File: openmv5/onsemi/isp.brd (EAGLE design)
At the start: 35.6 x 16.5 mm, 61 parts, among them IC1 AP0202AT2L00XPGA0, IC2 MIC5365-2.8YC5-TR, IC3 TLV62568PDDCR, J1 DF12-36-DS, J2 DF12-36-DP, M1 9774030151R, M2 9774030151R, Q1 PMXB120EPEZ

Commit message: Update resistor value
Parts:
- R6: value 1K -> 10K
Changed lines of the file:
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@@
 <attribute name="VALUE" x="12.581" y="8.255" size="0.8128" layer="28" ratio="10" rot="MR270"/>
 </element>
-<element name="R6" library="rcl" library_urn="urn:adsk.eagle:library:334" package="R0402" package3d_urn="urn:adsk.eagle:package:23547/3" value="1K" x="10.287" y="10.795" smashed="yes" rot="MR90">
-<attribute name="MPN" value="CRCW04021K00FKEDC" x="10.287" y="10.795" size="1.778" layer="28" rot="MR90" display="off"/>
+<element name="R6" library="rcl" library_urn="urn:adsk.eagle:library:334" package="R0402" package3d_urn="urn:adsk.eagle:package:23547/3" value="10K" x="10.287" y="10.795" smashed="yes" rot="MR90">
+<attribute name="MPN" value="AC0402FR-1310KL" x="10.287" y="10.795" size="1.778" layer="28" rot="MR90" display="off"/>
 <attribute name="NAME" x="10.922" y="10.16" size="1.27" layer="26" rot="MR90"/>
 <attribute name="POPULARITY" value="34" x="10.287" y="10.795" size="1.778" layer="28" rot="MR90" display="off"/>

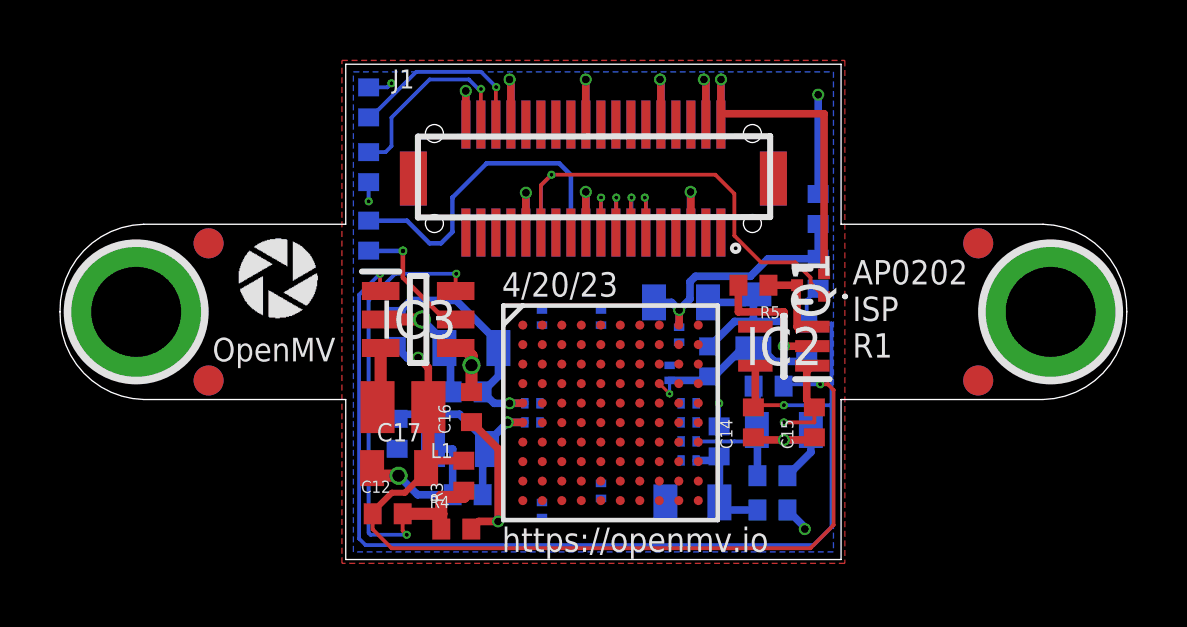
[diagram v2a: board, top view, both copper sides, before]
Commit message: Update camera modules to use different non-flippable pmosfet
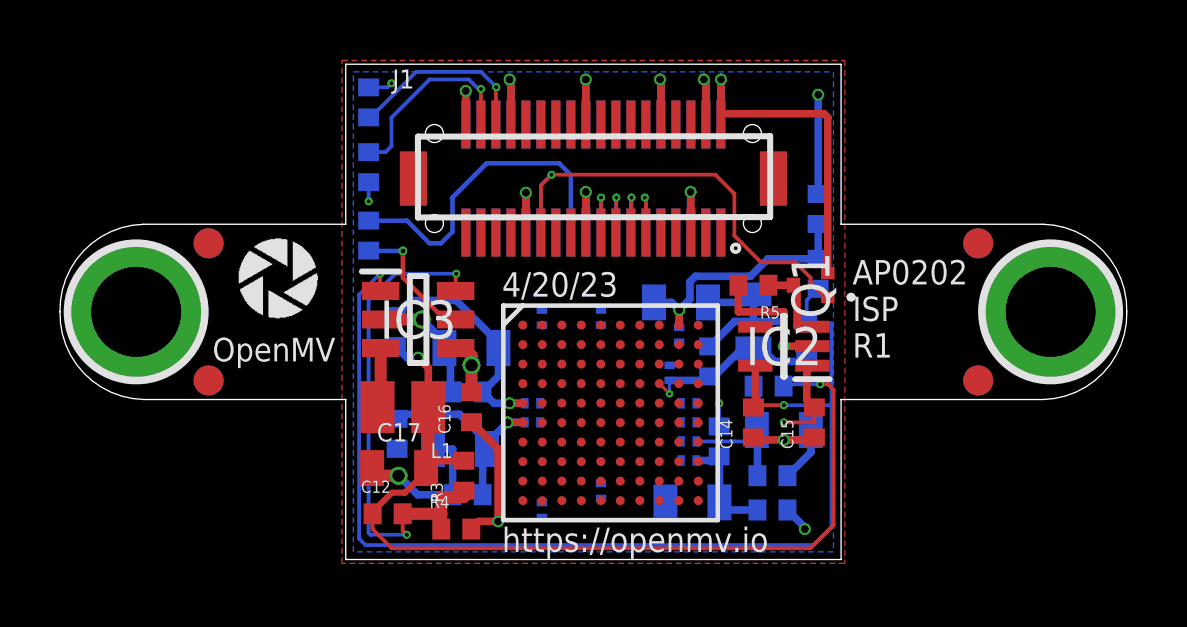
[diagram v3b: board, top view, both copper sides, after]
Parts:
- Q1: value PMXB120EPEZ -> SSM3J15FV,L3F; device PMXB120EPEZ:PMXB120EPEZ -> SSM3J15FV_L3F:SSM3J15FVL3F
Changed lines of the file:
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@@
 <attribute name="VALUE" x="21.082" y="2.794" size="0.6096" layer="28" font="vector" ratio="20" rot="MR180" align="top-center"/>
 </element>
-<element name="Q1" library="PMXB120EPEZ" package="PMXB120EPEZ" value="PMXB120EPEZ" x="25.019" y="9.144" smashed="yes" rot="R90">
-<attribute name="DESCRIPTION" value="MOSFET 30 V, P-channel Trench MOSFET" x="25.019" y="6.096" size="1.778" layer="27" rot="R90" display="off"/>
-<attribute name="HEIGHT" value="0.4mm" x="25.019" y="6.096" size="1.778" layer="27" rot="R90" display="off"/>
-<attribute name="MANUFACTURER_NAME" value="Nexperia" x="25.019" y="6.096" size="1.778" layer="27" rot="R90" display="off"/>
-<attribute name="MANUFACTURER_PART_NUMBER" value="PMXB120EPEZ" x="25.019" y="6.096" size="1.778" layer="27" rot="R90" display="off"/>
-<attribute name="MOUSER_PART_NUMBER" value="771-PMXB120EPEZ" x="25.019" y="6.096" size="1.778" layer="27" rot="R90" display="off"/>
-<attribute name="MOUSER_PRICE-STOCK" value="https://www.mouser.co.uk/ProductDetail/Nexperia/PMXB120EPEZ?qs=gNSudQoqUYCYLaOobF3dPA%3D%3D" x="25.019" y="6.096" size="1.778" layer="27" rot="R90" display="off"/>
-<attribute name="MPN" value="PMXB120EPEZ" x="25.019" y="6.096" size="1.778" layer="27" rot="R90" display="off"/>
+<element name="Q1" library="SSM3J15FV_L3F" package="SSM3J15FVL3F" value="SSM3J15FV,L3F" x="25.019" y="9.144" smashed="yes" rot="R90">
+<attribute name="DESCRIPTION" value="MOSFET Small-signal MOSFET High Speed Switching" x="25.019" y="6.096" size="1.778" layer="27" rot="R90" display="off"/>
+<attribute name="HEIGHT" value="0.55mm" x="25.019" y="6.096" size="1.778" layer="27" rot="R90" display="off"/>
+<attribute name="MANUFACTURER_NAME" value="Toshiba" x="25.019" y="6.096" size="1.778" layer="27" rot="R90" display="off"/>
+<attribute name="MANUFACTURER_PART_NUMBER" value="SSM3J15FV,L3F" x="25.019" y="6.096" size="1.778" layer="27" rot="R90" display="off"/>
+<attribute name="MOUSER_PART_NUMBER" value="757-SSM3J15FVL3F" x="25.019" y="6.096" size="1.778" layer="27" rot="R90" display="off"/>
+<attribute name="MOUSER_PRICE-STOCK" value="https://www.mouser.co.uk/ProductDetail/Toshiba/SSM3J15FVL3F?qs=PDgMCp4xDJb4qTgE7FAUzA%3D%3D" x="25.019" y="6.096" size="1.778" layer="27" rot="R90" display="off"/>
+<attribute name="MPN" value="SSM3J15FV,L3F" x="25.019" y="6.096" size="1.778" layer="27" rot="R90" display="off"/>
 <attribute name="NAME" x="25.019" y="9.144" size="1.27" layer="25" rot="R90" align="center"/>
 <attribute name="VALUE" x="25.019" y="9.144" size="1.27" layer="27" rot="R90" align="center"/>
@@
 </element>
 <element name="J1" library="DF12-36-DS" package="DF12-36-DS" value="DF12-36-DS" x="17.78" y="12.7" smashed="yes">
-<attribute name="MPN" value="DF12NB-36DS-0.5V(51)" x="17.78" y="12.7" size="1.778" layer="27" display="off"/>
+<attribute name="MPN" value="DF12NB(3.0)-36DS-0.5V(51)" x="17.78" y="12.7" size="1.778" layer="27" display="off"/>
 <attribute name="NAME" x="11.08" y="15.7" size="0.635" layer="25"/>
 </element>
@@
 <wire x1="25.146" y1="5.072" x2="24.892" y2="5.326" width="0.254" layer="1"/>
 <wire x1="24.892" y1="6.274" x2="24.892" y2="5.326" width="0.254" layer="1"/>
-<wire x1="25.469" y1="9.519" x2="25.469" y2="14.859" width="0.254" layer="1"/>
 <wire x1="22.03" y1="14.859" x2="22.03" y2="14.5001" width="0.254" layer="1"/>
-<wire x1="25.469" y1="14.859" x2="22.03" y2="14.859" width="0.254" layer="1"/>
+<wire x1="22.03" y1="14.859" x2="25.469" y2="14.859" width="0.254" layer="1"/>
 <wire x1="24.13" y1="4.572" x2="25.146" y2="4.572" width="0.127" layer="1"/>
 <wire x1="25.146" y1="4.572" x2="25.146" y2="5.072" width="0.127" layer="1"/>
@@
 <via x="24.8285" y="1.016" extent="1-16" drill="0.254"/>
 <wire x1="24.8285" y1="1.016" x2="24.8285" y2="1.031" width="0.254" layer="1"/>
-<wire x1="13.716" y1="5.58" x2="11.2395" y2="3.691" width="0" layer="19" extent="1-16"/>
+<wire x1="25.469" y1="14.859" x2="25.594" y2="14.734" width="0.254" layer="1"/>
+<wire x1="25.594" y1="14.734" x2="25.594" y2="9.544" width="0.254" layer="1"/>
+<wire x1="20.03" y1="14.5001" x2="22.03" y2="14.5001" width="0" layer="19" extent="16-16"/>
+<wire x1="17.526" y1="16.002" x2="20.0025" y2="16.002" width="0" layer="19" extent="1-1"/>
+<wire x1="15.03" y1="14.5001" x2="17.53" y2="14.5001" width="0" layer="19" extent="1-16"/>
+<wire x1="13.53" y1="14.5001" x2="15.03" y2="14.5001" width="0" layer="19" extent="1-16"/>
+<wire x1="11.049" y1="15.875" x2="13.5255" y2="15.621" width="0" layer="19" extent="1-1"/>
+<wire x1="25.08" y1="6.462" x2="25.594" y2="9.544" width="0" layer="19" extent="1-1"/>
+<wire x1="24.249" y1="1.651" x2="24.13" y2="4.572" width="0" layer="19" extent="16-16"/>
+<wire x1="10.287" y1="12.581" x2="10.287" y2="15.74" width="0" layer="19" extent="16-16"/>
+<wire x1="13.188" y1="7.051" x2="10.287" y2="11.938" width="0" layer="19" extent="1-1"/>
+<wire x1="11.2395" y1="3.691" x2="13.716" y2="5.58" width="0" layer="19" extent="1-16"/>
 </signal>
 <signal name="DCMI_D2" class="4">
@@
 <wire x1="23.368" y1="9.906" x2="24.511" y2="9.906" width="0.127" layer="1"/>
 <wire x1="24.511" y1="9.906" x2="25.019" y2="9.398" width="0.127" layer="1"/>
-<wire x1="25.019" y1="9.219" x2="25.469" y2="8.769" width="0.127" layer="1"/>
 <wire x1="21.844" y1="12.827" x2="22.479" y2="12.192" width="0.127" layer="1"/>
 <wire x1="25.019" y1="9.398" x2="25.019" y2="9.219" width="0.127" layer="1"/>
@@
 <via x="16.383" y="12.827" extent="1-16" drill="0.127"/>
 <wire x1="16.383" y1="12.827" x2="16.03" y2="12.474" width="0.127" layer="1"/>
+<wire x1="25.019" y1="9.219" x2="25.494" y2="8.744" width="0.127" layer="1"/>
+<wire x1="25.494" y1="8.744" x2="25.594" y2="8.744" width="0.127" layer="1"/>
 <wire x1="16.7265" y1="5.2145" x2="16.03" y2="10.8999" width="0" layer="19" extent="1-16"/>
 </signal>
@@
 <contactref element="R5" pad="1"/>
 <contactref element="Q1" pad="3"/>
-<wire x1="23.614" y1="9.144" x2="24.569" y2="9.144" width="0.254" layer="1"/>
-<wire x1="24.569" y1="9.144" x2="24.569" y2="7.762" width="0.254" layer="1"/>
+<wire x1="23.614" y1="9.144" x2="24.444" y2="9.144" width="0.254" layer="1"/>
 <wire x1="24.569" y1="7.762" x2="25.08" y2="7.762" width="0.254" layer="1"/>
+<wire x1="24.444" y1="9.144" x2="24.569" y2="9.019" width="0.254" layer="1"/>
+<wire x1="24.569" y1="9.019" x2="24.569" y2="7.762" width="0.254" layer="1"/>
 </signal>
 <signal name="VDDIO_S" class="3">
